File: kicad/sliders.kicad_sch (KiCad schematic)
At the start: 12 parts, among them U1 L293D, U2 L293D, U3 L293D, U5 L293D

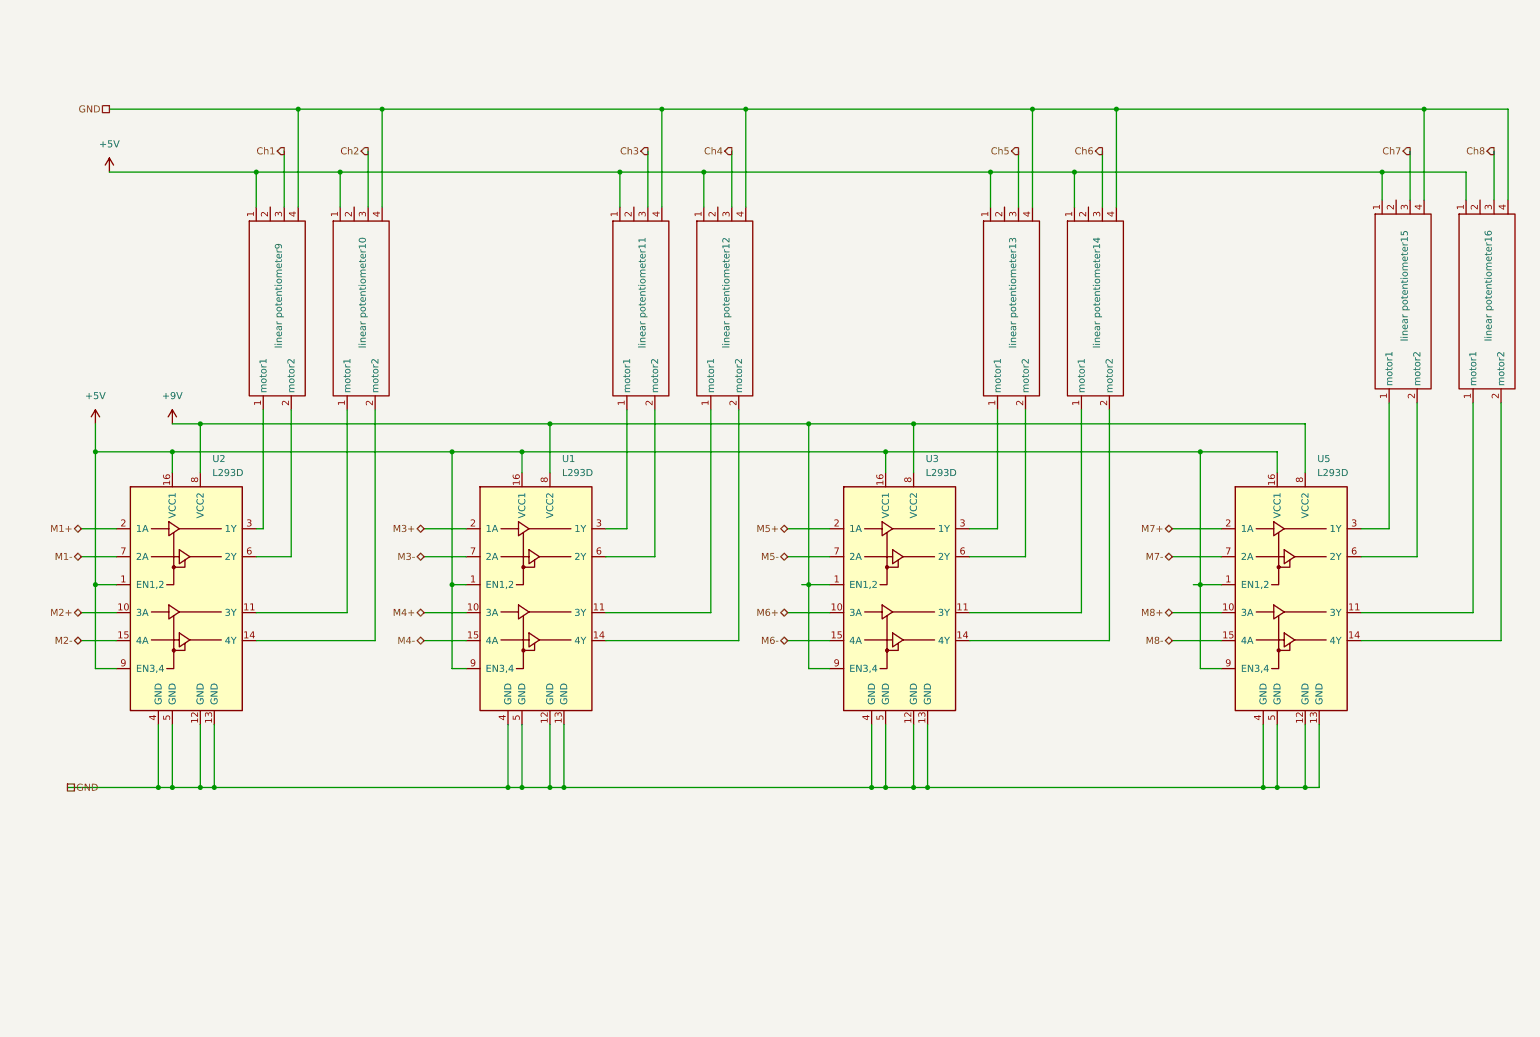
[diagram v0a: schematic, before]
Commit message: gain, meter and display sheets
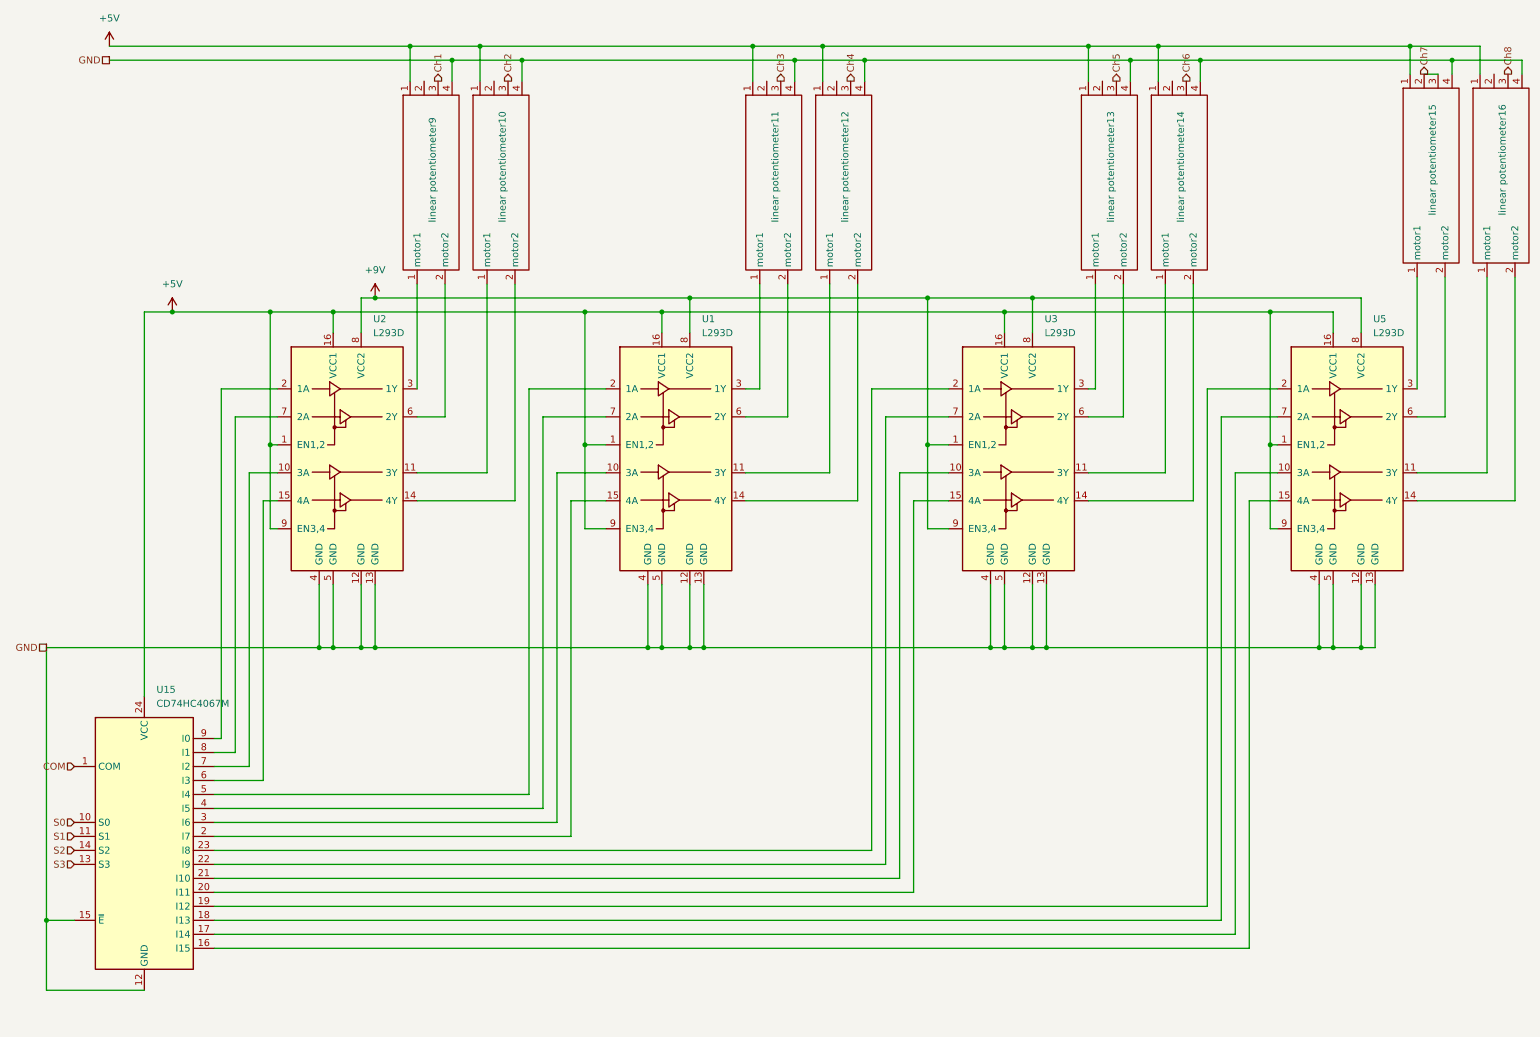
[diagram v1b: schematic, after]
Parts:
- added U15: CD74HC4067M, Package_SO:SOIC-24W_7.5x15.4mm_P1.27mm, symbol 74xx:CD74HC4067M
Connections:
- net +5V: now also U15.24 (VCC)
- net Ch7: now also linear potentiometer15.2 (motor2)
- net GND: now also U15.12 (GND), U15.15 (~{E})
- net at linear potentiometer13.2 (motor2): now also U3.6 (2Y)
- net at linear potentiometer11.2 (motor2): now also U1.6 (2Y)
- net at linear potentiometer12.2 (motor2): now also U1.14 (4Y)
- net at linear potentiometer9.2 (motor2): now also U2.6 (2Y)
- net M1+: no longer names the net of U2.2 (1A)
- net M1+: now also U15.9 (I0)
- net M1-: no longer names the net of U2.7 (2A)
- net M1-: now also U15.8 (I1)
- net M2+: no longer names the net of U2.10 (3A)
- net M2+: now also U15.7 (I2)
- net M2-: no longer names the net of U2.15 (4A)
- net M2-: now also U15.6 (I3)
- net M3+: no longer names the net of U1.2 (1A)
- net M3+: now also U15.5 (I4)
- net M3-: no longer names the net of U1.7 (2A)
- net M3-: now also U15.4 (I5)
- net M4+: no longer names the net of U1.10 (3A)
- net M4+: now also U15.3 (I6)
- net M4-: no longer names the net of U1.15 (4A)
- net M4-: now also U15.2 (I7)
- net M5+: no longer names the net of U3.2 (1A)
- net M5+: now also U15.23 (I8)
- net M5-: no longer names the net of U3.7 (2A)
- net M5-: now also U15.22 (I9)
- net M6+: no longer names the net of U3.10 (3A)
- net M6+: now also U15.21 (I10)
- net M6-: no longer names the net of U3.15 (4A)
- net M6-: now also U15.20 (I11)
- net M7+: no longer names the net of U5.2 (1A)
- net M7+: now also U15.19 (I12)
- net M7-: no longer names the net of U5.7 (2A)
- net M7-: now also U15.18 (I13)
- net M8+: no longer names the net of U5.10 (3A)
- net M8+: now also U15.17 (I14)
- net M8-: no longer names the net of U5.15 (4A)
- net M8-: now also U15.16 (I15)
- new net COM: U15.1 (COM)
- new net S0: U15.10 (S0)
- new net S1: U15.11 (S1)
- new net S2: U15.14 (S2)
- new net S3: U15.13 (S3)
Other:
- moved on the sheet: U1, U2, U3, U5, linear potentiometer10, linear potentiometer11, linear potentiometer12, linear potentiometer13, linear potentiometer14, linear potentiometer15, linear potentiometer16, linear potentiometer9

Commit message: kicad updates
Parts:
- added C3, C4, C5, C6, C7: 100nF, Capacitor_THT:C_Axial_L5.1mm_D3.1mm_P7.50mm_Horizontal, symbol Device:C
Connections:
- net +5V: now also linear potentiometer10.2 (motor2), linear potentiometer11.2 (motor2), linear potentiometer12.2 (motor2), linear potentiometer13.3, linear potentiometer14.3, linear potentiometer15.3, linear potentiometer16.3, linear potentiometer9.2 (motor2), C3.2, C4.2, C5.2, C6.2, C7.2; no longer linear potentiometer10.1 (motor1), linear potentiometer11.1 (motor1), linear potentiometer12.1 (motor1), linear potentiometer13.1 (motor1), linear potentiometer14.1 (motor1), linear potentiometer15.1 (motor1), linear potentiometer16.1 (motor1), linear potentiometer9.1 (motor1)
- net Ch1: now also linear potentiometer9.1 (motor1); no longer linear potentiometer9.3
- net Ch2: now also linear potentiometer10.1 (motor1); no longer linear potentiometer10.3
- net Ch3: now also linear potentiometer11.1 (motor1); no longer linear potentiometer11.3
- net Ch4: now also linear potentiometer12.1 (motor1); no longer linear potentiometer12.3
- net Ch5: now also linear potentiometer13.1 (motor1); no longer linear potentiometer13.3
- net Ch6: now also linear potentiometer14.1 (motor1); no longer linear potentiometer14.3
- net Ch7: now also linear potentiometer15.1 (motor1); no longer linear potentiometer15.2 (motor2), linear potentiometer15.3
- net Ch8: now also linear potentiometer16.1 (motor1); no longer linear potentiometer16.3
- net GND: now also C3.1, C4.1, C5.1, C6.1, C7.1
- net at linear potentiometer13.2 (motor2): now also U3.6 (2Y)

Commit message: pcb routing 1
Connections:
- net at linear potentiometer13.2 (motor2): now also U3.6 (2Y)
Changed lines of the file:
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@@
 	)
 	(symbol
-		(lib_name "mixer:motorised_linear_potentiometer")
 		(lib_id "mixer:motorised_linear_potentiometer")
 		(at 207.01 34.29 0)
@@
 	)
 	(symbol
-		(lib_name "mixer:motorised_linear_potentiometer")
 		(lib_id "mixer:motorised_linear_potentiometer")
 		(at 146.05 34.29 0)
@@
 	)
 	(symbol
-		(lib_name "mixer:motorised_linear_potentiometer")
 		(lib_id "mixer:motorised_linear_potentiometer")
 		(at 219.71 34.29 0)
@@
 	)
 	(symbol
-		(lib_name "mixer:motorised_linear_potentiometer")
 		(lib_id "mixer:motorised_linear_potentiometer")
 		(at 158.75 34.29 0)
@@
 	)
 	(symbol
-		(lib_name "mixer:motorised_linear_potentiometer")
 		(lib_id "mixer:motorised_linear_potentiometer")
 		(at 83.82 34.29 0)
@@
 	)
 	(symbol
-		(lib_name "mixer:motorised_linear_potentiometer")
 		(lib_id "mixer:motorised_linear_potentiometer")
 		(at 96.52 34.29 0)
@@
 	)
 	(symbol
-		(lib_name "mixer:motorised_linear_potentiometer")
 		(lib_id "mixer:motorised_linear_potentiometer")
 		(at 265.43 33.02 0)
@@
 	)
 	(symbol
-		(lib_name "mixer:motorised_linear_potentiometer")
 		(lib_id "mixer:motorised_linear_potentiometer")
 		(at 278.13 33.02 0)

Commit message: esp idf testing
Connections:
- net at linear potentiometer13.2 (motor2): now also U3.6 (2Y)
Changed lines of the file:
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@@
 (kicad_sch
-	(version 20231120)
+	(version 20250114)
 	(generator "eeschema")
-	(generator_version "8.0")
+	(generator_version "9.0")
 	(paper "A4")
 	(junction
@@
 		(shape input)
 		(at 19.05 162.56 180)
-		(fields_autoplaced yes)
 		(effects
 			(font
@@
 		(shape output)
 		(at 203.2 25.4 90)
-		(fields_autoplaced yes)
 		(effects
 			(font
@@
 		(shape input)
 		(at 19.05 149.86 180)
-		(fields_autoplaced yes)
 		(effects
 			(font
@@
 		(shape output)
 		(at 261.62 24.13 90)
-		(fields_autoplaced yes)
 		(effects
 			(font
@@
 		(shape input)
 		(at 19.05 160.02 180)
-		(fields_autoplaced yes)
 		(effects
 			(font
@@
 		(shape output)
 		(at 154.94 25.4 90)
-		(fields_autoplaced yes)
 		(effects
 			(font
@@
 		(shape output)
 		(at 274.32 24.13 90)
-		(fields_autoplaced yes)
 		(effects
 			(font
@@
 		(shape input)
 		(at 19.05 165.1 180)
-		(fields_autoplaced yes)
 		(effects
 			(font
@@
 		(shape output)
 		(at 215.9 25.4 90)
-		(fields_autoplaced yes)
 		(effects
 			(font
@@
 		(shape output)
 		(at 92.71 25.4 90)
-		(fields_autoplaced yes)
 		(effects
 			(font
@@
 		(shape output)
 		(at 142.24 25.4 90)
-		(fields_autoplaced yes)
 		(effects
 			(font
@@
 		(shape input)
 		(at 19.05 167.64 180)
-		(fields_autoplaced yes)
 		(effects
 			(font
@@
 		(shape output)
 		(at 80.01 25.4 90)
-		(fields_autoplaced yes)
 		(effects
 			(font
